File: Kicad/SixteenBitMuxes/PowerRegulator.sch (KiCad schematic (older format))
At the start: 11 parts, among them J5 PowerTest_PinHeader, J6 9V Power JST XH, U1 AMS1117-5.0, U2 AMS1117-3.3

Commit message: PCB mostly
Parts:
- C3, C4: footprint Capacitor_THT:CP_Radial_D5.0mm_P2.50mm -> Diode_SMD:D_SMB_Handsoldering
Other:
- note added: "22 uF Tantalum advised ->\n47 uf Tantalum in inventory instead"
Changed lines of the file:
@@
 Text Notes 3250 2300 0    20   ~ 0
 9 mA, 81 mW
-Text Notes 4950 2050 0    31   ~ 0
+Text Notes 4950 1900 0    31   ~ 0
 5V: LCD: about 60 mA\nPd = (9 V - 5V) * 60 mA = 240 mW\nTj = Ta(max) + Pd * (Thermal Resistance (junction-to-ambient) =\n125 = 30 + Pd * 70 => 1.36 W\nNo heat sink needed
-Text Notes 4950 3100 0    31   ~ 0
+Text Notes 4950 2900 0    31   ~ 0
 3.3V: STM32: about 100 mA \nPd = (9 V - 3.3V) * 100 mA = 570 mW\nTj = Ta(max) + Pd * (Thermal Resistance (junction-to-ambient) =\n125 = 30 + Pd * 70 => 1.36 W\nNo heat sink needed
 Connection ~ 3550 2850
@@
 F 0 "C4" H 4665 3046 50  0000 L CNN
 F 1 "22uF" H 4665 2955 50  0000 L CNN
-F 2 "Capacitor_THT:CP_Radial_D5.0mm_P2.50mm" H 4550 3000 50  0001 C CNN
+F 2 "Diode_SMD:D_SMB_Handsoldering" H 4550 3000 50  0001 C CNN
 F 3 "~" H 4550 3000 50  0001 C CNN
 	1    4550 3000
@@
 F 0 "C3" H 4665 1996 50  0000 L CNN
 F 1 "22uF" H 4665 1905 50  0000 L CNN
-F 2 "Capacitor_THT:CP_Radial_D5.0mm_P2.50mm" H 4550 1950 50  0001 C CNN
+F 2 "Diode_SMD:D_SMB_Handsoldering" H 4550 1950 50  0001 C CNN
 F 3 "~" H 4550 1950 50  0001 C CNN
 	1    4550 1950
@@
 	1150 2300 1450 2300
 Connection ~ 1150 2300
+Text Notes 4950 2100 0    31   ~ 0
+22 uF Tantalum advised ->\n47 uf Tantalum in inventory instead
+Text Notes 4950 3100 0    31   ~ 0
+22 uF Tantalum advised ->\n47 uf Tantalum in inventory instead
 $EndSCHEMATC

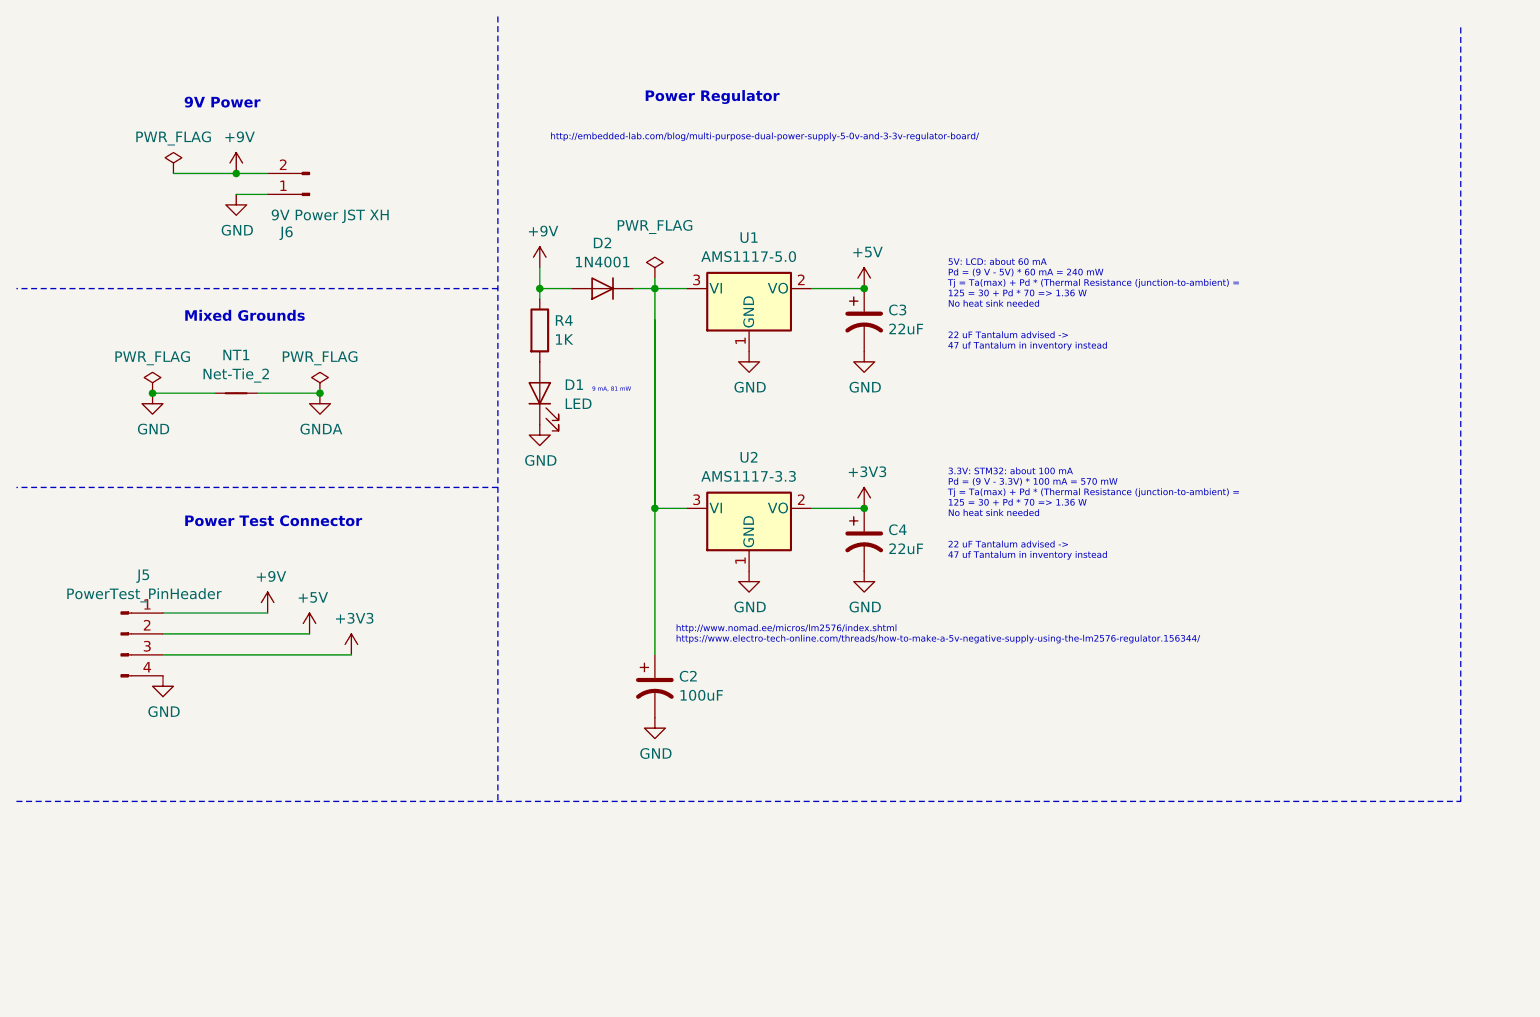
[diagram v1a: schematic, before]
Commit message: Code + resistors
Many code changes (UI) + resistors -> pulldowns.
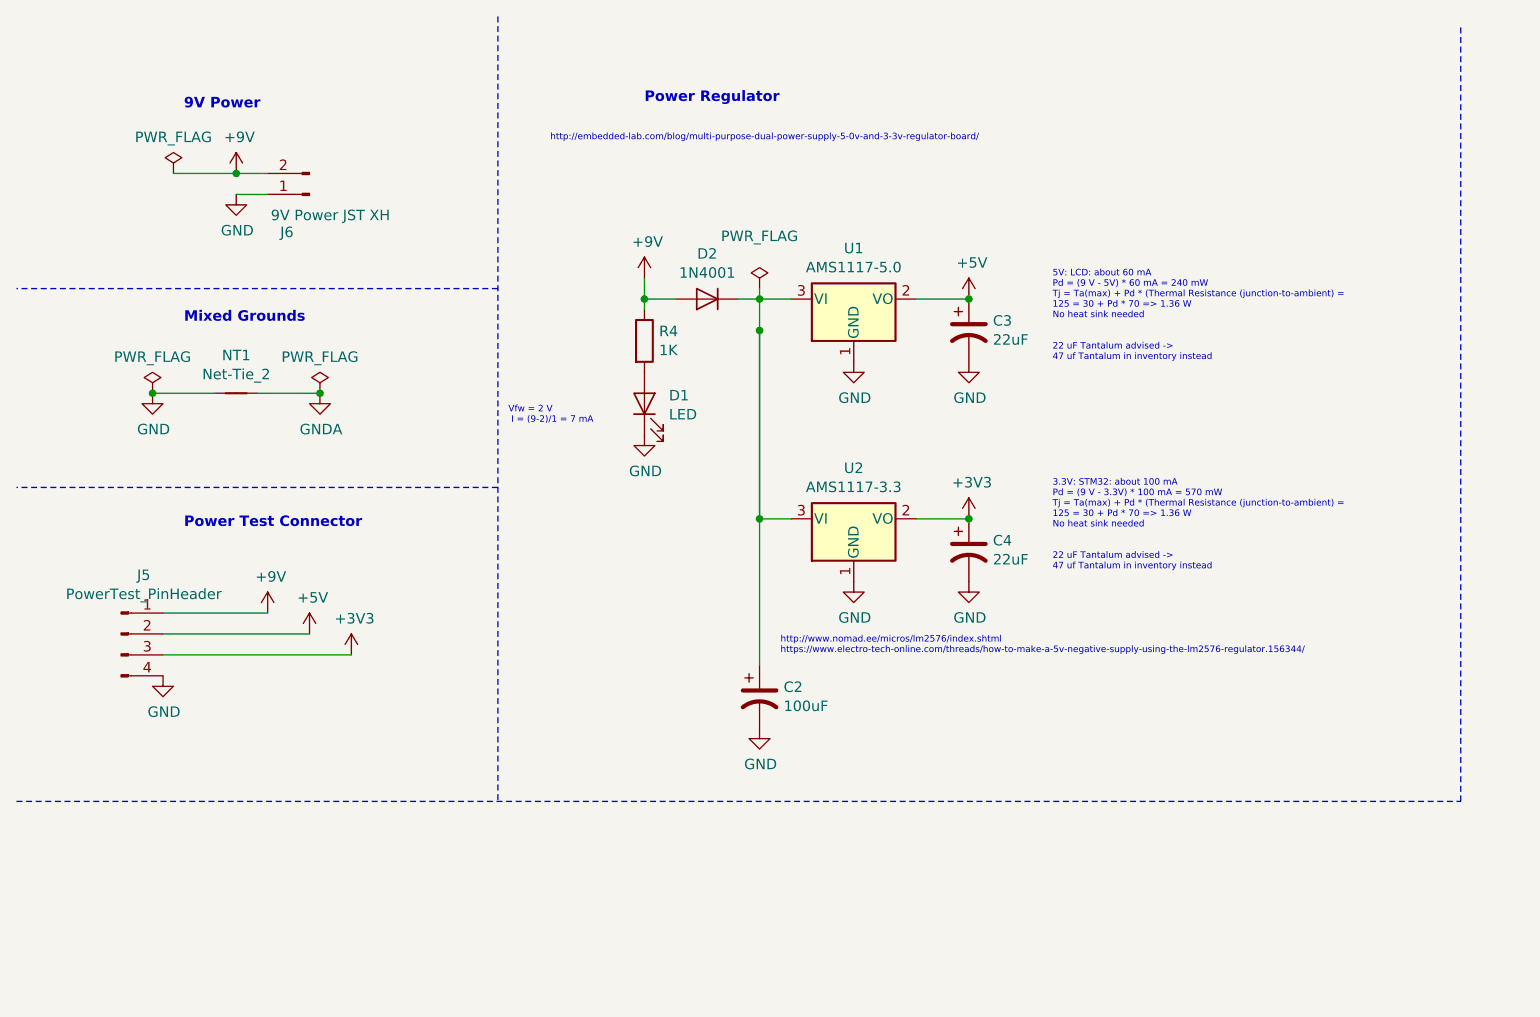
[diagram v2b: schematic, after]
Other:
- note added: "Vfw = 2 V\n I = (9-2)/1 = 7 mA"
- note removed: "9 mA, 81 mW"
- moved on the sheet: C2, C3, C4, D1, D2, R4, U1, U2

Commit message: Improvements according video youtube
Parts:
- added F1: Polyfuse 1.1A (1812), Inductor_SMD:L_1812_4532Metric_Pad1.30x3.40mm_HandSolder, symbol Device:Polyfuse
- added FB1: 1K, 100MHz, Inductor_SMD:L_0805_2012Metric_Pad1.15x1.40mm_HandSolder, symbol Device:Ferrite_Bead
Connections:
- net labels added: +9V_SAFE
- wire segments 20 -> 21
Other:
- moved on the sheet: C2, C3, C4, D1, D2, R4, U1, U2

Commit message: Various
Various
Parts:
- F1: value Polyfuse 1.1A (1812) -> Polyfuse 1.1A (1812L)
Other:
- note added: "Model: BLM21AG102SN1D'\nSpecs: 600 mA, 25% 1 KOhm, 100 MHz, 0805\nAccording AliExpress: 200 mA"
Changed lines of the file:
@@
 	7400 5200 550  5200
-$Comp
-L Device:Polyfuse F1
-U 1 1 5EC30FA0
-P 3550 2100
-F 0 "F1" H 3638 2146 50  0000 L CNN
-F 1 "Polyfuse 1.1A (1812)" H 3638 2055 50  0000 L CNN
-F 2 "Inductor_SMD:L_1812_4532Metric_Pad1.30x3.40mm_HandSolder" H 3600 1900 50  0001 L CNN
-F 3 "~" H 3550 2100 50  0001 C CNN
-	1    3550 2100
-	1    0    0    -1
-$EndComp
 $Comp
 L Device:Ferrite_Bead FB1
@@
 Wire Wire Line
 	3800 2800 4100 2800
+$Comp
+L Device:Polyfuse F1
+U 1 1 5EC30FA0
+P 3550 2100
+F 0 "F1" H 3638 2146 50  0000 L CNN
+F 1 "Polyfuse 1.1A (1812L)" H 3638 2055 50  0000 L CNN
+F 2 "Inductor_SMD:L_1812_4532Metric_Pad1.30x3.40mm_HandSolder" H 3600 1900 50  0001 L CNN
+F 3 "~" H 3550 2100 50  0001 C CNN
+	1    3550 2100
+	1    0    0    -1
+$EndComp
+Text Notes 4250 2500 0    50   ~ 0
+Model: BLM21AG102SN1D'\nSpecs: 600 mA, 25% 1 KOhm, 100 MHz, 0805\nAccording AliExpress: 200 mA
 $EndSCHEMATC
